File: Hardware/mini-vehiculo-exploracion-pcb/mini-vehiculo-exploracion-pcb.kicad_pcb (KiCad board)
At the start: 2 copper layers, 92 x 79 mm, 83 parts, among them IC3 MAX8891EXK33_V+T, J1 CÁMARA, J3 UJ20-C-H-G-SMT-5-P16-TR, J8 SERVO, Q1 SI1467DH-T1-BE3, U2 ESP32-S3-WROOM-1, U3 LM358, U4 TPS561208DDCR

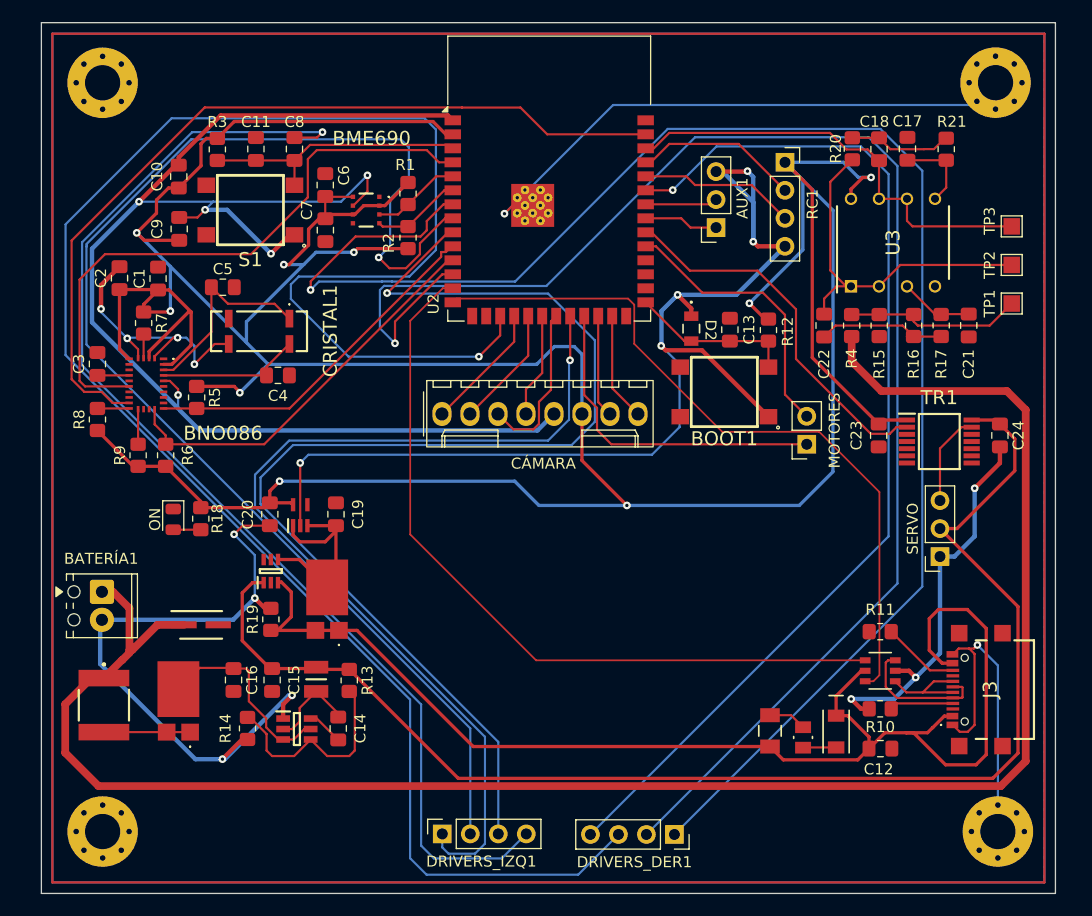
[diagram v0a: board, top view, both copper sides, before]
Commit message: Add hardware to main
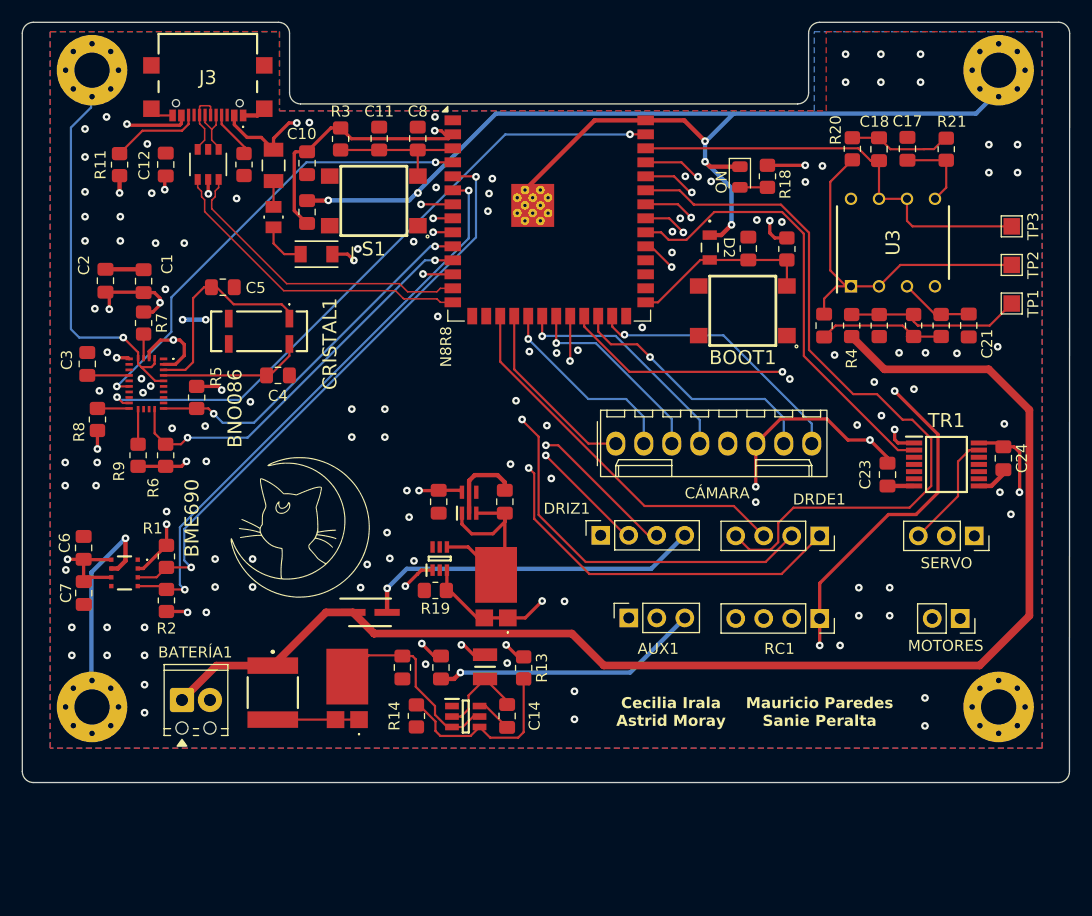
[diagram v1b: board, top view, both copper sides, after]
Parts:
- added G***: LOGO, luna_sailormoon, F.Cu at (108.5, 87.8)
- moved J3 90.5 mm to (100.1, 46.7), turned to 180 degrees
- moved C12 83.7 mm to (96.3, 54.9), turned to 90 degrees
- moved R11 81.0 mm to (92.1, 54.9), turned to -90 degrees
- moved CR1 76.3 mm to (100.2, 54.9), turned to -90 degrees
- moved R10 76.0 mm to (103.4, 54.9), turned to -90 degrees
- moved F1 68.3 mm to (106.1, 55.0), turned to -90 degrees
- moved FB1 67.4 mm to (106.1, 59.6)
- moved D1 64.0 mm to (110.0, 63.0), turned to 180 degrees
- moved D6 60.1 mm to (148.4, 56.0)
- moved R18 60.1 mm to (150.9, 55.9)
- moved RC1 41.5 mm to (155.7, 96.1), turned to -90 degrees
- moved C6 39.6 mm to (88.9, 89.7)
- moved BME690 39.6 mm to (92.6, 91.9)
- moved C7 39.6 mm to (88.9, 93.7)
- moved R1 39.6 mm to (96.4, 90.4)
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- renumbered DRIVERS_DER1 to DRDE1, DRIVERS_IZQ1 to DRIZ1, U2 to N8R8
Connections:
- CR1 pad 1: /MCU_Peripherals/D+ -> /MCU_Peripherals/D-
- CR1 pad 3: /MCU_Peripherals/D- -> /MCU_Peripherals/D+
- CR1 pad 4: USB_D- -> USB_D+
- CR1 pad 6: USB_D+ -> USB_D-
- F1 pad 1: V_BUS -> /MCU_Peripherals/V_BUS1
- J3 pad A4: V_BUS -> /MCU_Peripherals/V_BUS1
- J3 pad B4: V_BUS -> /MCU_Peripherals/V_BUS1
- J3 pad MP1: unconnected-(J3-PadMP1) -> GND
- J3 pad MP2: unconnected-(J3-PadMP2) -> GND
- J3 pad MP3: unconnected-(J3-PadMP3) -> GND
- J3 pad MP4: unconnected-(J3-PadMP4) -> GND
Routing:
- net GND: track 544.9 -> 245.7 mm, vias 24 -> 128
- net +3.3V: track 350.0 -> 130.2 mm, vias 9 -> 19
- net /M1_DISABLE: track 179.9 -> 34.6 mm, vias 1 -> 0
- net /M1_IN2: track 138.3 -> 55.2 mm, vias 1 -> 2
- net /M1_IN1: track 149.7 -> 67.1 mm, vias 1 -> 2
- net /M2_IN2: track 122.1 -> 42.3 mm, vias 1 -> 2
- net /M2_DISABLE: track 110.0 -> 41.8 mm, vias 1 -> 2
- net /M2_IN1: track 87.8 -> 21.0 mm
- net /M2_nFAULT: track 25.2 -> 71.7 mm, vias 0 -> 1
- net /SDA1: track 8.09 -> 54.0 mm, vias 0 -> 2
- net /SCL1: track 8.15 -> 53.1 mm, vias 0 -> 2
- net ENT_BAT: track 166.3 -> 121.6 mm
- net USB_D-: track 70.5 -> 28.0 mm
- net V_BUS: track 116.8 -> 77.1 mm, vias 0 -> 4
- net /PIN_AUX2: track 6.57 -> 43.5 mm, vias 0 -> 1
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- added copper zone on In2.Cu, net +3.3V
- added copper zone on In1.Cu, net GND
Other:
- board size 92 x 79 mm -> 95 x 69 mm
- copper layers 2 -> 4
- board text added: "Cecilia Irala Astrid Moray"
- board text added: "Mauricio Paredes Sanie Peralta"
